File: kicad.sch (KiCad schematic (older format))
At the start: 23 parts, among them J1 Screw_Terminal_01x02, J2 Screw_Terminal_01x03, J3 Screw_Terminal_01x03, J4 Conn_01x05, J5 Screw_Terminal_01x03, J9 Conn_01x03, SW1 SW_Push, SW2 SW_Push, U11 DS1233A-10, U12 PCF8574, U6 ESP32

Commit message: cambios varios, agregado esp-12e
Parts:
- removed H1, H2: MountingHole_Pad, MountingHole:MountingHole_4mm_Pad_Via, symbol Mechanical:MountingHole_Pad
- removed J9: Conn_01x03, Connector_Molex:Molex_KK-254_AE-6410-03A_1x03_P2.54mm_Vertical, symbol Connector_Generic:Conn_01x03
- removed U12: PCF8574, Package_SO:SOIC-16W_7.5x10.3mm_P1.27mm, symbol Interface_Expansion:PCF8574
- removed U6: ESP32, esp32-wroom-roover:ESP32-WROOM-WROVER-NC, symbol RF_Module:ESP32-WROOM-32
- added R? (x2): 10k, Resistor_SMD:R_1206_3216Metric, symbol Device:R
- added U?: ESP-12E, ESP8266:ESP-12E_SMD, symbol ESP8266:ESP-12E
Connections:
- net +3V3: now also R?.1, U?.3 (CH_PD), U?.8 (VCC)
- net GND: now also R?.2, U?.9 (GND)
- net GPIO0: now also U?.12 (GPIO0)
- net RELAY_1: now also U?.5 (GPIO14)
- net RELAY_2: now also U?.6 (GPIO12)
- net RELAY_3: now also U?.7 (GPIO13)
- net RESET: now also U?.1 (REST), U?.4 (GPIO16)
- net RXD0: now also U?.15 (RXD)
- net SCL: now also U?.14 (GPIO5)
- net SDA: now also U?.13 (GPIO4)
- net TXD0: now also U?.16 (TXD)
- new net: R?.1, U?.10 (GPIO15)
- new net: R?.2, U?.11 (GPIO2)
- new net TEMP: U?.2 (ADC)
- no-connect marks 16 -> 6
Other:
- note added: "TEMPERATURE SENSOR"
- note removed: "CURRENT SENSOR"
- note removed: "POWER OUTPUT"
- note removed: "TEMPERATURE SENSORS"
- note removed: "ups_carga"
- note removed: "ups_inverter"
- note removed: "ups_normal"
- note removed: "ups_on"
- moved on the sheet: C1, C22

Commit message: esquema anotado
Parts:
- gave numbers to parts that had none: 3
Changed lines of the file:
@@
 $EndComp
 $Comp
-L ESP8266:ESP-12E U?
+L ESP8266:ESP-12E U2
 U 1 1 61514EB0
 P 8950 6100
-F 0 "U?" H 8950 6865 50  0000 C CNN
+F 0 "U2" H 8950 6865 50  0000 C CNN
 F 1 "ESP-12E" H 8950 6774 50  0000 C CNN
 F 2 "ESP8266:ESP-12E_SMD" H 8950 6100 50  0001 C CNN
@@
 	2350 2950 2350 3650
 $Comp
-L Device:R R?
+L Device:R R15
 U 1 1 61652449
 P 10250 6000
-F 0 "R?" H 10320 6046 50  0000 L CNN
+F 0 "R15" H 10320 6046 50  0000 L CNN
 F 1 "10k" H 10320 5955 50  0000 L CNN
 F 2 "Resistor_SMD:R_1206_3216Metric" V 10180 6000 50  0001 C CNN
@@
 	9850 6300 10250 6300
 $Comp
-L power:+3V3 #PWR?
+L power:+3V3 #PWR05
 U 1 1 61656891
 P 10250 5750
-F 0 "#PWR?" H 10250 5600 50  0001 C CNN
+F 0 "#PWR05" H 10250 5600 50  0001 C CNN
 F 1 "+3V3" H 10265 5923 50  0000 C CNN
 F 2 "" H 10250 5750 50  0001 C CNN
@@
 	10250 6150 10250 6300
 $Comp
-L Device:R R?
+L Device:R R20
 U 1 1 6166E9AD
 P 10250 6650
-F 0 "R?" H 10320 6696 50  0000 L CNN
+F 0 "R20" H 10320 6696 50  0000 L CNN
 F 1 "10k" H 10320 6605 50  0000 L CNN
 F 2 "Resistor_SMD:R_1206_3216Metric" V 10180 6650 50  0001 C CNN
@@
 $EndComp
 $Comp
-L power:GND #PWR?
+L power:GND #PWR011
 U 1 1 6166F7A3
 P 10250 6900
-F 0 "#PWR?" H 10250 6650 50  0001 C CNN
+F 0 "#PWR011" H 10250 6650 50  0001 C CNN
 F 1 "GND" H 10255 6727 50  0000 C CNN
 F 2 "" H 10250 6900 50  0001 C CNN

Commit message: demasiados cambios mi loco
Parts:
- removed D1, D2: SS14, Diode_SMD:D_SMA_Handsoldering, symbol Diode:B140-E3
- removed J1: Screw_Terminal_01x02, libs:TerminalBlock_bornier-2_P5.08mm, symbol Connector:Screw_Terminal_01x02
- removed J3, J5: Screw_Terminal_01x03, libs:TerminalBlock_bornier-3_P5.08mm, symbol Connector:Screw_Terminal_01x03
- removed R5: 22k, Resistor_SMD:R_1206_3216Metric, symbol Device:R
- removed R6: 5k6, Resistor_SMD:R_1206_3216Metric, symbol Device:R
- removed U11: DS1233A-10, Package_TO_SOT_THT:TO-92, symbol components:DS1233
- added C1, C2: 100nF, Capacitor_SMD:C_1206_3216Metric_Pad1.33x1.80mm_HandSolder, symbol Device:C
- added J3: ICSP, Connector_PinSocket_2.54mm:PinSocket_1x06_P2.54mm_Vertical, symbol Connector_Generic:Conn_01x06
- added U1, U2: ADS1115IDGS, Package_SO:TSSOP-10_3x3mm_P0.5mm, symbol Analog_ADC:ADS1115IDGS
- renumbered C1 to C3, C22 to C4, J2 to J1, J4 to J2, R11 to R3, R12 to R4, R15 to R5, R20 to R6, U2 to U3
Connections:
- net +3V3: now also C1.1, C2.1, J3.6 (Pin_6), U1.8 (VDD), U2.1 (ADDR), U2.8 (VDD)
- net GND: now also C1.2, C2.2, J3.5 (Pin_5), U1.1 (ADDR), U1.3 (GND), U2.3 (GND)
- net GPIO0: now also J3.4 (Pin_4)
- net RESET: now also J3.1 (Pin_1)
- net RXD0: now also J3.3 (Pin_3)
- net SCL: now also U1.10 (SCL), U2.10 (SCL)
- net SDA: now also U1.9 (SDA), U2.9 (SDA)
- net TXD0: now also J3.2 (Pin_2)
- net RELAY_2 renamed RDY1
- net RDY1: now also U1.2 (ALERT/RDY), U2.2 (ALERT/RDY)
- net RELAY_3 renamed RDY2
- no-connect marks 6 -> 10
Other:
- note added: "0x48"
- note added: "0x49"
- note added: "ICSP HEADER"
- note removed: "*Optional."
- note removed: "POWER MONITOR"
- note removed: "POWER SUPPLY"
- note removed: "USB Power"
- moved on the sheet: J1

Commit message: quiero dormir culiaaaa
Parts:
- removed U1, U2: ADS1115IDGS, Package_SO:TSSOP-10_3x3mm_P0.5mm, symbol Analog_ADC:ADS1115IDGS
- added C1, C5: 470uF, libs:CAP_10x10_SMD_THT, symbol Device:CP
- added C3: 1uF, Capacitor_SMD:C_1206_3216Metric_Pad1.33x1.80mm_HandSolder, symbol Device:C
- added C4, C6: 100nF, Capacitor_SMD:C_1206_3216Metric_Pad1.33x1.80mm_HandSolder, symbol Device:C
- added D1, D2, D3: LED, LED_SMD:LED_1206_3216Metric, symbol Device:LED
- added D4, D5: M7, Diode_SMD:D_SMA_Handsoldering, symbol Diode:1N4007
- added J1, J3: Screw_Terminal_01x02, libs:TerminalBlock_bornier-2_P5.08mm, symbol Connector:Screw_Terminal_01x02
- added J2: jack3.5mm, Connector_Audio:Jack_3.5mm_Ledino_KB3SPRS_Horizontal, symbol Connector:AudioPlug3
- added J5: Conn_01x03, Connector_Molex:Molex_KK-254_AE-6410-03A_1x03_P2.54mm_Vertical, symbol Connector_Generic:Conn_01x03
- added J7: Screw_Terminal_01x03, libs:TerminalBlock_bornier-3_P5.08mm, symbol Connector:Screw_Terminal_01x03
- added K1, K2: RELAY 0510, Relay_THT:Relay_SPDT_SANYOU_SRD_Series_Form_C, symbol Relay:SANYOU_SRD_Form_C
- added PS1: HLK-PM01, Converter_ACDC:Converter_ACDC_HiLink_HLK-PMxx, symbol Converter_ACDC:HLK-PM01
- added Q1, Q2: BC817, Package_TO_SOT_SMD:SOT-23, symbol Transistor_BJT:BC817
- added R1, R2: 100k, Resistor_SMD:R_1206_3216Metric, symbol Device:R
- added R10, R11: 10k, Resistor_SMD:R_1206_3216Metric, symbol Device:R
- added R12, R13, R9: 220, Resistor_SMD:R_1206_3216Metric, symbol Device:R
- added R14, R15, R7: 1k, Resistor_SMD:R_1206_3216Metric, symbol Device:R
- added R8: ?, Resistor_SMD:R_1206_3216Metric, symbol Device:R
- added T1: ZMPT101B, ZMPT101B:ZMPT101B, symbol ZMPT101B:ZMPT101B
- added U1: KF33BD-TR, Package_SO:SO-8_3.9x4.9mm_P1.27mm, symbol kf33:KF33BD-TR
- added U2: ADS1015IDGS, Package_SO:TSSOP-10_3x3mm_P0.5mm, symbol Analog_ADC:ADS1015IDGS
- renumbered C1 to C7, C3 to C8, C4 to C9, J2 to J4, J3 to J6, J1 to J8, R5 to R16, R6 to R17, R1 to R5, R2 to R6
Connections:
- net +3V3: now also C5.1, C6.1, J5.1 (Pin_1), R10.1, U1.1 (VOUT), U2.8 (VDD); no longer C2.1
- net +5V: now also C2.1, C1.1, D1.2 (A), D2.2 (A), D3.2 (A), D4.1 (K), D5.1 (K), K1.5, K2.5, PS1.4 (+Vout), U1.8 (VIN)
- net GND: now also C1.2, C4.2, C5.2, C6.2, J5.3 (Pin_3), PS1.3 (-Vout), Q1.2 (E), Q2.2 (E), R11.2, R9.2, U1.2 (GND), U1.3 (GND), U1.5 (INH), U1.6 (GND), U1.7 (GND), U2.1 (ADDR), U2.3 (GND)
- net RELAY_1: now also R14.2
- net SCL: now also U2.10 (SCL)
- net SDA: now also U2.9 (SDA)
- net TEMP: now also C4.1, J5.2 (Pin_2)
- net RDY1 renamed RELAY_2
- net RELAY_2: now also R15.2
- net RDY2 renamed RDY
- net RDY: now also U2.2 (ALERT/RDY)
- net Relay 1/COM: no longer names the net of J8.2 (Pin_2)
- net Relay 1/COM: now also K2.1
- net Relay 1/NC: no longer names the net of J8.3 (Pin_3)
- net Relay 1/NC: now also K2.4
- net Relay 1/NO: no longer names the net of J8.1 (Pin_1)
- net Relay 1/NO: now also K2.3
- new net: Q2.1 (B), R15.1
- new net: D5.2 (A), K2.2, Q2.3 (C), R13.2
- new net: D3.1 (K), R13.1
- new net: D1.1 (K), R9.1
- new net: J1.1 (Pin_1), PS1.1 (AC/L), R1.2
- new net: J1.2 (Pin_2), PS1.2 (AC/N), T1.2
- new net: C3.2, U2.4 (AIN0)
- new net: J2.S, J3.1 (Pin_1), R8.1, U2.5 (AIN1)
- new net: J2.T, J3.2 (Pin_2), R10.2, R11.1, R7.1, R8.2, T1.4, U2.7 (AIN3)
- new net: J7.1 (Pin_1), K1.3
- new net: J7.2 (Pin_2), K1.1
- new net: J7.3 (Pin_3), K1.4
- new net: Q1.1 (B), R14.1
- new net: D4.2 (A), K1.2, Q1.3 (C), R12.2
- new net: D2.1 (K), R12.1
- new net: R2.1, T1.1
- new net: C3.1, R7.2, T1.3
- new net: R1.1, R2.2
- no-connect marks 10 -> 8
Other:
- note added: "LM35"
- note removed: "0x49"
- note removed: "ICSP HEADER"
- note removed: "PUSHBUTTONS"
- note removed: "RELAY OUTPUTS"
- note removed: "TEMPERATURE SENSOR"
- moved on the sheet: C7, C8, C9, J4, J6, J8, R16, R17, R3, R4, R5, R6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

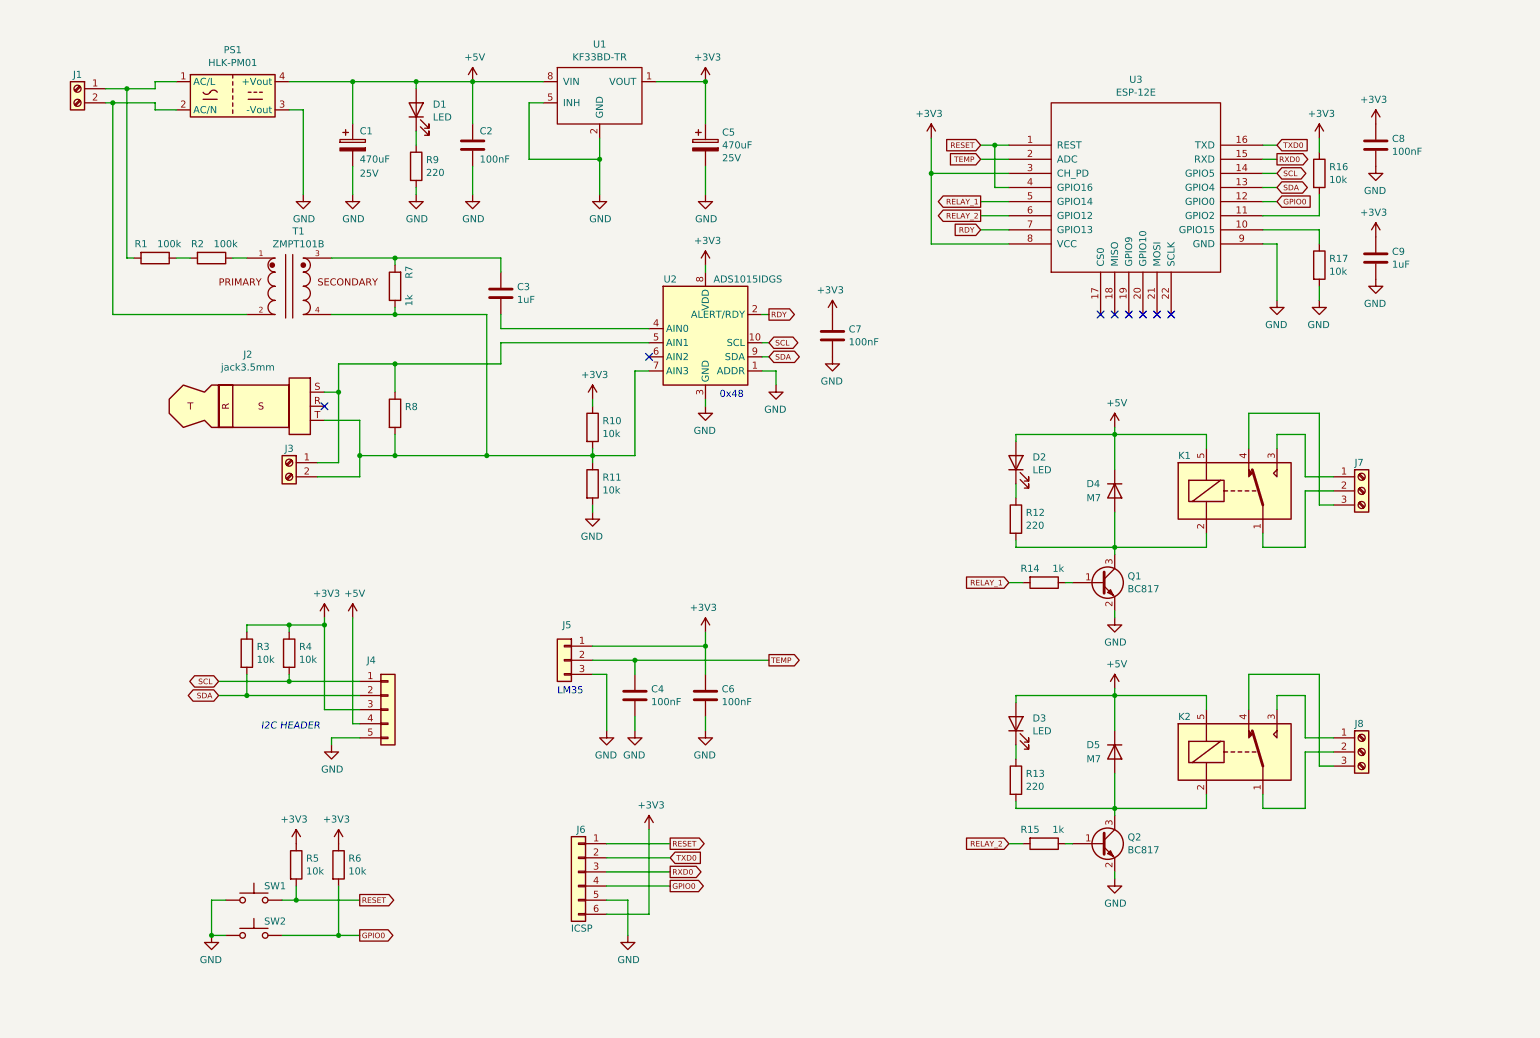
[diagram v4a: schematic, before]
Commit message: Esquematico final del proyecto.
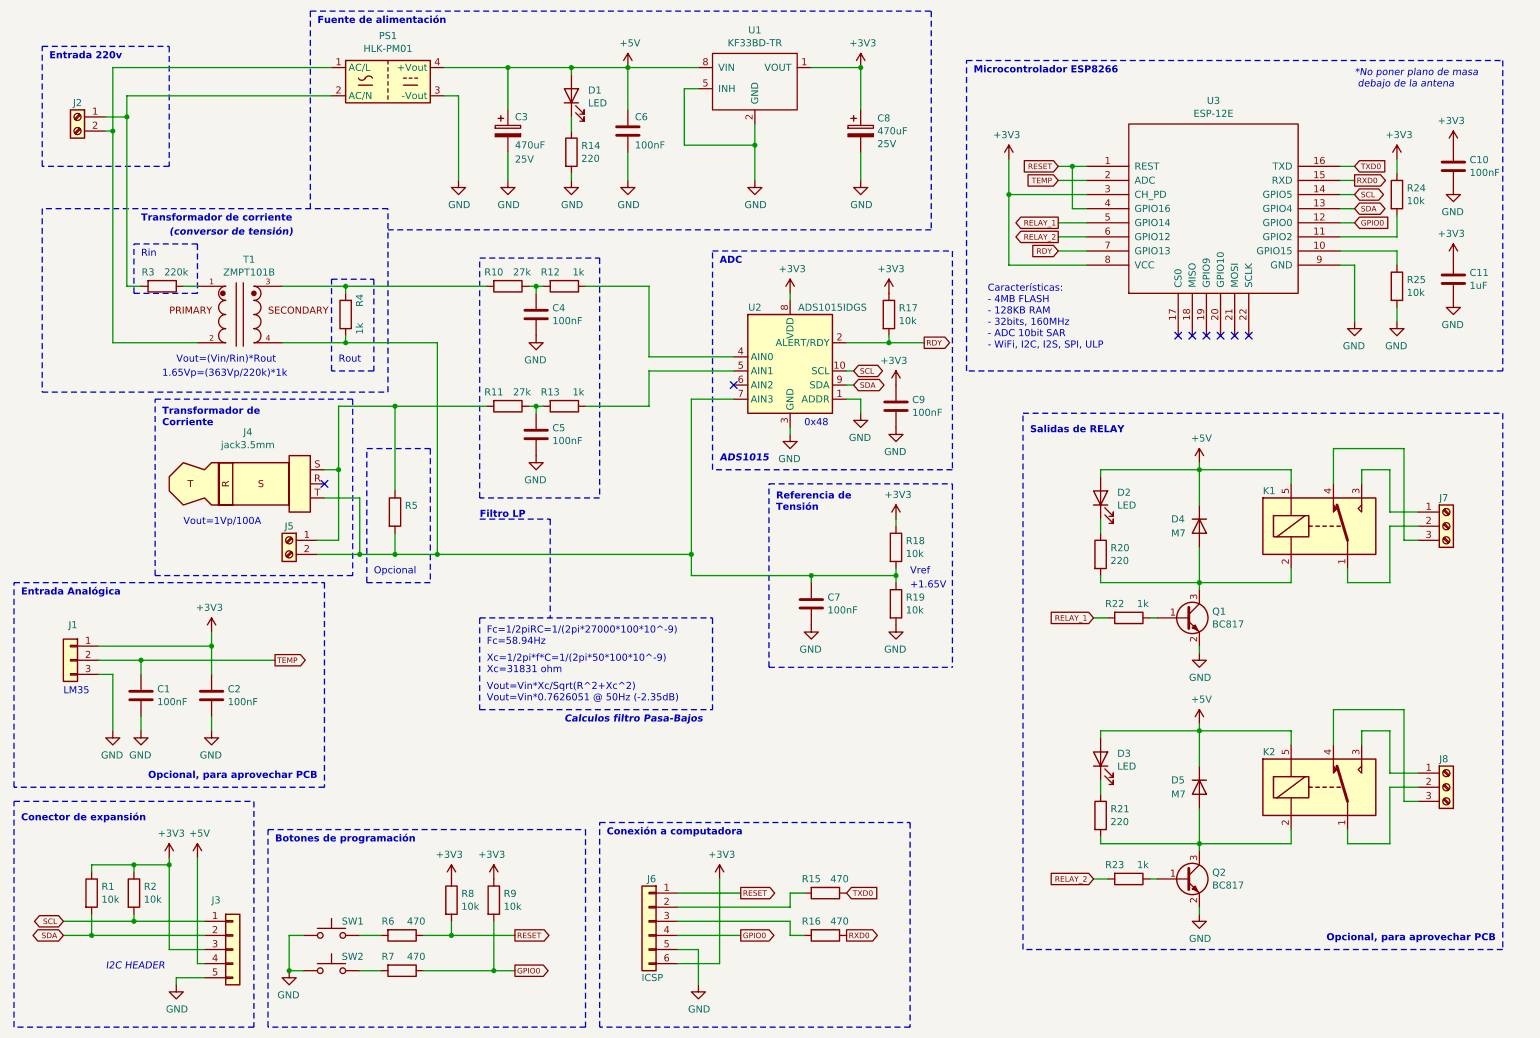
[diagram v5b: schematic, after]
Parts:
- removed C3: 1uF, Capacitor_SMD:C_1206_3216Metric_Pad1.33x1.80mm_HandSolder, symbol Device:C
- removed R1: 100k, Resistor_SMD:R_1206_3216Metric, symbol Device:R
- added C4, C5, C7: 100nF, Capacitor_SMD:C_1206_3216Metric_Pad1.33x1.80mm_HandSolder, symbol Device:C
- added R10, R11: 27k, Resistor_SMD:R_1206_3216Metric, symbol Device:R
- added R12, R13: 1k, Resistor_SMD:R_1206_3216Metric, symbol Device:R
- added R15, R16, R6, R7: 470, Resistor_SMD:R_1206_3216Metric, symbol Device:R
- added R17: 10k, Resistor_SMD:R_1206_3216Metric, symbol Device:R
- PS1: manf# (none) -> HLK-PM01
- R3: renamed from R2; value 100k -> 220k; manf# RC1206FR-07100KL -> RC1206FR-07220KL
- T1: manf# (none) -> ZMPT101B
- U1: manf# (none) -> KF33BD-TR
- U2: manf# (none) -> ADS1015IDGS
- renumbered C4 to C1, C8 to C10, C9 to C11, C6 to C2, C1 to C3, C2 to C6, C5 to C8, C7 to C9, J5 to J1, J1 to J2, J4 to J3, J2 to J4, J3 to J5, R3 to R1, R9 to R14, R10 to R18, R11 to R19, R4 to R2, R12 to R20, R13 to R21, R14 to R22, R15 to R23, R16 to R24, R17 to R25, R7 to R4, R8 to R5, R5 to R8, R6 to R9
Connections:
- net +3V3: now also R17.1
- net GND: now also C4.2, C5.2, C7.2
- net GPIO0: now also R7.1; no longer SW2.2
- net RDY: now also R17.2
- net RESET: now also R6.1; no longer SW1.2
- net RXD0: now also R16.1; no longer J6.3 (Pin_3)
- net TXD0: now also R15.1; no longer J6.2 (Pin_2)
- net at J2.1 (Pin_1): now also PS1.2 (AC/N), R3.2; no longer PS1.1 (AC/L)
- net at J2.2 (Pin_2), T1.2: now also PS1.1 (AC/L); no longer PS1.2 (AC/N)
- net at U2.4 (AIN0): now also R12.1
- net at J4.S, J5.1 (Pin_1), R5.1: now also R11.2; no longer U2.5 (AIN1)
- net at J4.T, J5.2 (Pin_2), R18.2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: now also C7.1
- net at R4.2, T1.3: now also R10.2
- new net: R7.2, SW2.2
- new net: R6.2, SW1.2
- new net: R13.1, U2.5 (AIN1)
- new net: C5.1, R11.1, R13.2
- new net: C4.1, R10.1, R12.2
- new net: J6.2 (Pin_2), R15.2
- new net: J6.3 (Pin_3), R16.2
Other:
- note added: "(conversor de tensión)"
- note added: "*No poner plano de masa\n debajo de la antena"
- note added: "+1.65V"
- note added: "1.65Vp=(363Vp/220k)*1k"
- note added: "ADC"
- note added: "ADS1015"
- note added: "Botones de programación"
- note added: "Calculos filtro Pasa-Bajos"
- note added: "Características:\n- 4MB FLASH\n- 128KB RAM\n- 32bits, 160MHz\n- ADC 10bit SAR\n- WiFi, I2C, I2S, SPI, ULP"
- note added: "Conector de expansión"
- note added: "Conexión a computadora"
- note added: "Entrada 220v"
- note added: "Entrada Analógica"
- note added: "Fc=1/2piRC=1/(2pi*27000*100*10^-9)\nFc=58.94Hz"
- note added: "Filtro LP"
- note added: "Fuente de alimentación"
- note added: "Microcontrolador ESP8266"
- note added: "Opcional"
- note added: "Opcional, para aprovechar PCB"
- note added: "Referencia de\nTensión"
- note added: "Rin"
- note added: "Rout"
- note added: "Salidas de RELAY"
- note added: "Transformador de corriente"
- note added: "Transformador de\nCorriente"
- note added: "Vout=(Vin/Rin)*Rout"
- note added: "Vout=1Vp/100A"
- note added: "Vout=Vin*Xc/Sqrt(R^2+Xc^2)\nVout=Vin*0.7626051 @ 50Hz (-2.35dB)"
- note added: "Vref"
- note added: "Xc=1/2pi*f*C=1/(2pi*50*100*10^-9)\nXc=31831 ohm"
- moved on the sheet: C1, C10, C11, C2, C3, C6, C8, C9, D1, D2, D3, D4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

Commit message: terminado ruteado principal
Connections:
- net at PS1.2 (AC/N), R3.2: now also J2.2 (Pin_2); no longer J2.1 (Pin_1)
- net at PS1.1 (AC/L), T1.2: now also J2.1 (Pin_1); no longer J2.2 (Pin_2)
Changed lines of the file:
@@
 L Connector:Screw_Terminal_01x02 J2
 U 1 1 6182613C
-P 1000 1300
+P 1000 1400
 AR Path="/6182613C" Ref="J2"  Part="1"
 AR Path="/60CF66AD/6182613C" Ref="J?"  Part="1"
-F 0 "J2" H 1000 1400 50  0000 C CNN
-F 1 "Screw_Terminal_01x02" H 918 1426 50  0001 C CNN
-F 2 "libs:TerminalBlock_bornier-2_P5.08mm" H 1000 1300 50  0001 C CNN
-F 3 "https://www.te.com/commerce/DocumentDelivery/DDEController?Action=srchrtrv&DocNm=796636&DocType=Customer+Drawing&DocLang=English" H 1000 1300 50  0001 C CNN
-F 4 "796636-2" H 1000 1300 50  0001 C CNN "manf#"
-	1    1000 1300
-	-1   0    0    -1
+F 0 "J2" H 1000 1200 50  0000 C CNN
+F 1 "Screw_Terminal_01x02" H 918 1526 50  0001 C CNN
+F 2 "libs:TerminalBlock_bornier-2_P5.08mm" H 1000 1400 50  0001 C CNN
+F 3 "https://www.te.com/commerce/DocumentDelivery/DDEController?Action=srchrtrv&DocNm=796636&DocType=Customer+Drawing&DocLang=English" H 1000 1400 50  0001 C CNN
+F 4 "796636-2" H 1000 1400 50  0001 C CNN "manf#"
+	1    1000 1400
+	-1   0    0    1
 $EndComp
 Wire Wire Line

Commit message: Exportar step, pick&place, sch, bom
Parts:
- T1: MANUFACTURER Qingxian Zeming Langxi Electronic -> (none); MAXIMUM_PACKAGE_HEIGHT 18.8mm -> (none); PARTREV NA -> (none); STANDARD Manufacturer Recommendations -> (none)
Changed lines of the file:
@@
 F 2 "ZMPT101B:ZMPT101B" H 2150 2700 50  0001 L BNN
 F 3 "" H 2150 2700 50  0001 L BNN
-F 4 "18.8mm" H 2150 2700 50  0001 L BNN "MAXIMUM_PACKAGE_HEIGHT"
-F 5 "Manufacturer Recommendations" H 2150 2700 50  0001 L BNN "STANDARD"
-F 6 "NA" H 2150 2700 50  0001 L BNN "PARTREV"
-F 7 "Qingxian Zeming Langxi Electronic" H 2150 2700 50  0001 L BNN "MANUFACTURER"
-F 8 "ZMPT101B" H 2150 2700 50  0001 C CNN "manf#"
+F 4 "ZMPT101B" H 2150 2700 50  0001 C CNN "manf#"
 	1    2150 2700
 	1    0    0    -1
